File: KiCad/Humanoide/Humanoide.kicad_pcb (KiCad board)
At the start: 2 copper layers, 50 x 50 mm, 119 parts, among them CON1 SPI, IC1 CP2102, P1 CONN_01X03, P10 USB_OTG, P11 SRV9, P12 SRV10, P13 SRV11, P14 SRV12, P15 SRV13, P16 SRV14, P17 SRV15, P18 SRV16, P19 SRV17, P2 SRV1, P20 SRV18, P21 SRV19, P22 SRV20, P23 I2C, P24 UART, P25 V_BATT, P26 USB_BT, P3 SRV2, P4 SRV3, P5 SRV4, P6 SRV5, P7 SRV6, P8 SRV7, P9 SRV8, Q1 IRF7842PBF, SW1 SW_PUSH, U1 LM3940IMP, U2 ATSAM3X8EA-AU, X1 CSTCE 12MHz, Y1 32.768kHz

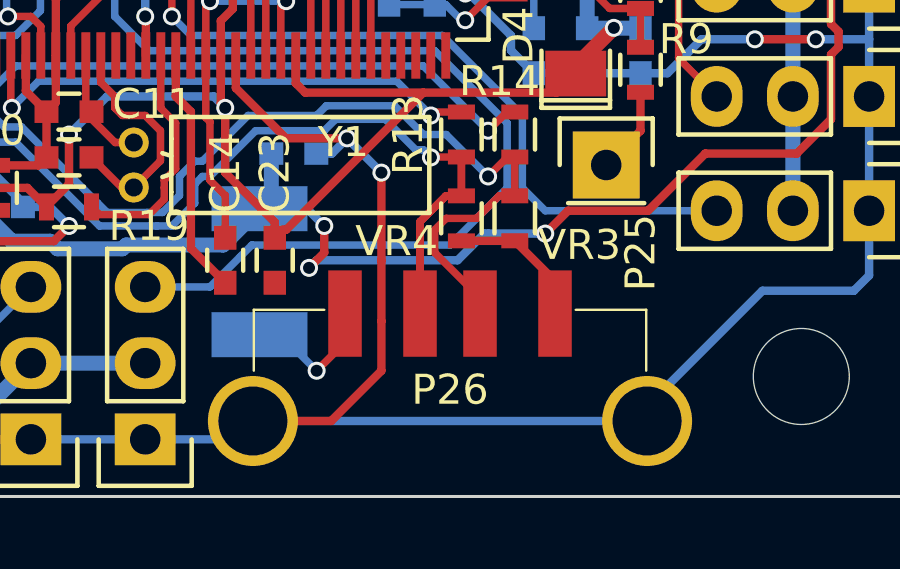
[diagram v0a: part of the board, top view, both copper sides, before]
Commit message: Kicad 3D model changed
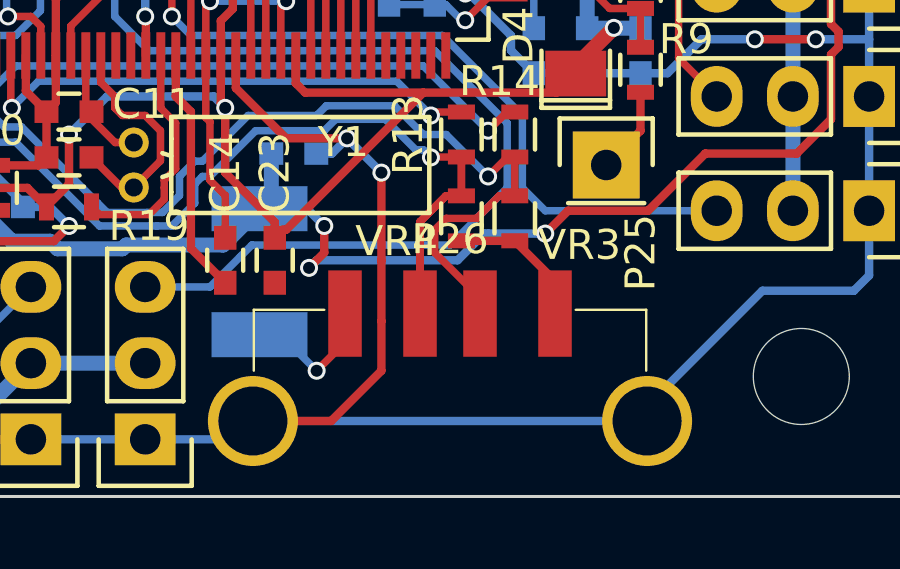
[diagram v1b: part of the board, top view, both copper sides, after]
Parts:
- P26: footprint Humanoide_lib:USB-B -> Humanoide_lib:USB-A-SMD
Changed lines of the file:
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@@
     (pad 2 smd rect (at 1.6525 0 270) (size 0.762 1.27) (layers B.Cu B.Paste B.Mask)
       (net 1 VCC))
-    (model "${KIPRJMOD}/shapes3D/diodo SS1P3L.wrl"
+    (model ${KIPRJMOD}/shapes3D/SS1P3L.wrl
       (at (xyz 0.077 0.045 0))
       (scale (xyz 0.3937 0.3937 0.3937))
@@
     (pad 2 smd rect (at 0 -2.1 270) (size 3.2 1.5) (layers B.Cu B.Paste B.Mask)
       (net 3 +5V))
-    (model "${KIPRJMOD}/shapes3D/PTC 500mA.wrl"
-      (at (xyz -0.06378 -0.08956699999999999 0))
+    (model ${KIPRJMOD}/shapes3D/mf-msmf050.wrl
+      (at (xyz 0 0 0))
       (scale (xyz 0.3937 0.3937 0.3937))
-      (rotate (xyz 270 0 270))
+      (rotate (xyz 90 0 0))
     )
   )
@@
     (pad 2 smd rect (at 0 -2.1 180) (size 3.2 1.5) (layers B.Cu B.Paste B.Mask)
       (net 29 "Net-(F2-Pad2)"))
-    (model "${KIPRJMOD}/shapes3D/PTC 500mA.wrl"
-      (at (xyz -0.06378 -0.08956699999999999 0))
+    (model ${KIPRJMOD}/shapes3D/mf-msmf050.wrl
+      (at (xyz 0 0 0))
       (scale (xyz 0.3937 0.3937 0.3937))
-      (rotate (xyz 270 0 270))
+      (rotate (xyz 90 0 0))
     )
   )
@@
     (pad 2 smd rect (at 1.35 0) (size 1.5 1.3) (layers B.Cu B.Paste B.Mask)
       (net 4 GND))
-    (model ${KIPRJMOD}/shapes3D/SMD-0805.wrl
-      (at (xyz 0 0 0))
-      (scale (xyz 0.1 0.1 0.1))
+    (model ${KIPRJMOD}/shapes3D/L_0805.wrl
+      (at (xyz 0 0 0))
+      (scale (xyz 0.3937 0.3937 0.3937))
       (rotate (xyz 0 0 0))
     )
@@
     (pad 2 smd rect (at 1.35 0 180) (size 1.5 1.3) (layers B.Cu B.Paste B.Mask)
       (net 13 "Net-(C21-Pad1)"))
-    (model ${KIPRJMOD}/shapes3D/SMD-0805.wrl
-      (at (xyz 0 0 0))
-      (scale (xyz 0.1 0.1 0.1))
+    (model ${KIPRJMOD}/shapes3D/L_0805.wrl
+      (at (xyz 0 0 0))
+      (scale (xyz 0.3937 0.3937 0.3937))
       (rotate (xyz 0 0 0))
     )
@@
     (pad 2 smd rect (at 1.35 0 180) (size 1.5 1.3) (layers B.Cu B.Paste B.Mask)
       (net 14 "Net-(C28-Pad2)"))
-    (model ${KIPRJMOD}/shapes3D/SMD-0805.wrl
-      (at (xyz 0 0 0))
-      (scale (xyz 0.1 0.1 0.1))
+    (model ${KIPRJMOD}/shapes3D/L_0805.wrl
+      (at (xyz 0 0 0))
+      (scale (xyz 0.3937 0.3937 0.3937))
       (rotate (xyz 0 0 0))
     )
@@
     (pad 2 smd rect (at 1.35 0 180) (size 1.5 1.3) (layers B.Cu B.Paste B.Mask)
       (net 15 VDDUTMI))
-    (model ${KIPRJMOD}/shapes3D/SMD-0805.wrl
-      (at (xyz 0 0 0))
-      (scale (xyz 0.1 0.1 0.1))
+    (model ${KIPRJMOD}/shapes3D/L_0805.wrl
+      (at (xyz 0 0 0))
+      (scale (xyz 0.3937 0.3937 0.3937))
       (rotate (xyz 0 0 0))
     )
@@
     (pad 2 smd rect (at 1.35 0) (size 1.5 1.3) (layers B.Cu B.Paste B.Mask)
       (net 16 VDDANA))
-    (model ${KIPRJMOD}/shapes3D/SMD-0805.wrl
-      (at (xyz 0 0 0))
-      (scale (xyz 0.1 0.1 0.1))
+    (model ${KIPRJMOD}/shapes3D/L_0805.wrl
+      (at (xyz 0 0 0))
+      (scale (xyz 0.3937 0.3937 0.3937))
       (rotate (xyz 0 0 0))
     )
@@
     (pad 6 smd rect (at 3.75 2.85) (size 2.3 1.9) (layers F.Cu F.Paste F.Mask)
       (net 43 "Net-(L1-Pad1)"))
-    (model ${KIPRJMOD}/shapes3D/micro-USB-smd.wrl
-      (at (xyz -3.857874 0.012 -0.016))
+    (model ${KIPRJMOD}/shapes3D/USB-micro-B.wrl
+      (at (xyz 0 -0.105 0))
       (scale (xyz 0.3937 0.3937 0.3937))
-      (rotate (xyz 270 0 0))
+      (rotate (xyz 0 0 270))
     )
   )
@@
     (pad 4 thru_hole oval (at 7.62 0) (size 2 2.6) (drill 1.2) (layers *.Cu *.Mask F.SilkS)
       (net 67 SCL))
-    (model ${KIPRJMOD}/shapes3D/molex-4-pines.wrl
+    (model ${KIPRJMOD}/shapes3D/22-29-2041.wrl
       (at (xyz 0.15 0 0.063))
       (scale (xyz 0.3937 0.3937 0.3937))
@@
     (pad 4 thru_hole oval (at 7.62 0) (size 2 2.6) (drill 1.2) (layers *.Cu *.Mask F.SilkS)
       (net 69 TX1))
-    (model ${KIPRJMOD}/shapes3D/molex-4-pines.wrl
+    (model ${KIPRJMOD}/shapes3D/22-29-2041.wrl
       (at (xyz 0.15 0 0.063))
       (scale (xyz 0.3937 0.3937 0.3937))
@@
       (scale (xyz 1 1 1))
       (rotate (xyz 0 0 90))
-    )
-  )
-  (module Humanoide_lib:USB-B (layer F.Cu)
-    (at 159.29 123.904)
-    (descr http://docs-europe.electrocomponents.com/webdocs/0fc0/0900766b80fc0369.pdf)
-    (tags "Connector USB SMD")
-    (fp_text reference P26 (at 0 2.54) (layer F.SilkS)
-      (effects (font (size 1 1) (thickness 0.15)))
-    )
-    (fp_text value USB_BT (at 0 2.7305) (layer F.Fab) hide
-      (effects (font (size 1 1) (thickness 0.15)))
-    )
-    (fp_line (start 6.5405 13.843) (end 6.5405 5.2705) (layer Dwgs.User) (width 0.08))
-    (fp_line (start -6.5405 13.843) (end -6.5405 5.2705) (layer Dwgs.User) (width 0.08))
-    (fp_line (start 6.5405 -0.127) (end 6.5405 1.905) (layer F.SilkS) (width 0.08))
-    (fp_line (start -4.191 -0.127) (end -6.5405 -0.127) (layer F.SilkS) (width 0.08))
-    (fp_line (start -6.5405 -0.127) (end -6.5405 1.905) (layer F.SilkS) (width 0.08))
-    (fp_line (start 6.5405 -0.127) (end 4.191 -0.127) (layer F.SilkS) (width 0.08))
-    (fp_line (start 6.5405 13.843) (end -6.5405 13.843) (layer Dwgs.User) (width 0.08))
-    (pad 1 smd rect (at -3.5 0) (size 1.12 2.88) (layers F.Cu F.Paste F.Mask)
-      (net 29 "Net-(F2-Pad2)"))
-    (pad 2 smd rect (at -1 0) (size 1.12 2.88) (layers F.Cu F.Paste F.Mask)
-      (net 71 D-))
-    (pad 3 smd rect (at 1 0) (size 1.12 2.88) (layers F.Cu F.Paste F.Mask)
-      (net 72 D+))
-    (pad 4 smd rect (at 3.5 0) (size 1.12 2.88) (layers F.Cu F.Paste F.Mask)
-      (net 4 GND))
-    (pad 5 thru_hole circle (at -6.57 3.58) (size 3 3) (drill 2.3) (layers *.Cu *.Mask F.SilkS)
-      (net 4 GND))
-    (pad 5 thru_hole circle (at 6.57 3.58) (size 3 3) (drill 2.3) (layers *.Cu *.Mask F.SilkS)
-      (net 4 GND))
-    (model ${KIPRJMOD}/shapes3D/USB_A_SMD.wrl
-      (at (xyz 0 -0.23 0.08))
-      (scale (xyz 3 3 3))
-      (rotate (xyz 270 0 0))
     )
   )
@@
     (pad 3 smd rect (at 1.2 0 270) (size 0.6 2) (layers F.Cu F.Paste F.Mask)
       (net 121 "Net-(U2-Pad36)"))
-    (model "${KIPRJMOD}/shapes3D/resonador CSTCC.wrl"
-      (at (xyz -0.06299 0.0256 0))
-      (scale (xyz 0.17 0.1778 0.170603))
-      (rotate (xyz -90 0 0))
+    (model ${KIPRJMOD}/shapes3D/CSTCE.wrl
+      (at (xyz 0 0 0))
+      (scale (xyz 400 400 400))
+      (rotate (xyz 0 0 0))
     )
   )
@@
     (pad 2 thru_hole circle (at 0.7493 0 270) (size 1.00076 1.00076) (drill 0.59944) (layers *.Cu *.Mask F.SilkS)
       (net 9 "Net-(C10-Pad1)"))
-    (model "${KIPRJMOD}/shapes3D/Crystal 32kHz.wrl"
-      (at (xyz 0.04 0.275 -0.08))
+    (model ${KIPRJMOD}/shapes3D/TC38H.wrl
+      (at (xyz 0 0.058 0.06))
       (scale (xyz 0.3937 0.3937 0.3937))
-      (rotate (xyz -90 0 90))
+      (rotate (xyz -90 180 180))
     )
   )
@@
     (pad 1 np_thru_hole circle (at 0 0) (size 3.2 3.2) (drill 3.2) (layers *.Cu *.Mask F.SilkS))
   )
+  (module Humanoide_lib:USB-A-SMD (layer F.Cu)
+    (at 159.29 123.904)
+    (descr http://docs-europe.electrocomponents.com/webdocs/0fc0/0900766b80fc0369.pdf)
+    (tags "Connector USB SMD")
+    (fp_text reference P26 (at 0 -2.4765) (layer F.SilkS)
+      (effects (font (size 1 1) (thickness 0.15)))
+    )
+    (fp_text value USB_BT (at 0 2.7305) (layer F.Fab)
+      (effects (font (size 1 1) (thickness 0.15)))
+    )
+    (fp_line (start 6.5405 13.843) (end 6.5405 5.2705) (layer Dwgs.User) (width 0.08))
+    (fp_line (start -6.5405 13.843) (end -6.5405 5.2705) (layer Dwgs.User) (width 0.08))
+    (fp_line (start 6.5405 -0.127) (end 6.5405 1.905) (layer F.SilkS) (width 0.08))
+    (fp_line (start -4.191 -0.127) (end -6.5405 -0.127) (layer F.SilkS) (width 0.08))
+    (fp_line (start -6.5405 -0.127) (end -6.5405 1.905) (layer F.SilkS) (width 0.08))
+    (fp_line (start 6.5405 -0.127) (end 4.191 -0.127) (layer F.SilkS) (width 0.08))
+    (fp_line (start 6.5405 13.843) (end -6.5405 13.843) (layer Dwgs.User) (width 0.08))
+    (pad 1 smd rect (at -3.5 0) (size 1.12 2.88) (layers F.Cu F.Paste F.Mask)
+      (net 29 "Net-(F2-Pad2)"))
+    (pad 2 smd rect (at -1 0) (size 1.12 2.88) (layers F.Cu F.Paste F.Mask)
+      (net 71 D-))
+    (pad 3 smd rect (at 1 0) (size 1.12 2.88) (layers F.Cu F.Paste F.Mask)
+      (net 72 D+))
+    (pad 4 smd rect (at 3.5 0) (size 1.12 2.88) (layers F.Cu F.Paste F.Mask)
+      (net 4 GND))
+    (pad 5 thru_hole circle (at -6.57 3.58) (size 3 3) (drill 2.3) (layers *.Cu *.Mask F.SilkS)
+      (net 4 GND))
+    (pad 5 thru_hole circle (at 6.57 3.58) (size 3 3) (drill 2.3) (layers *.Cu *.Mask F.SilkS)
+      (net 4 GND))
+    (model ${KIPRJMOD}/shapes3D/USB_A_SMD.wrl
+      (at (xyz 0 -0.23 0.055))
+      (scale (xyz 2.54 2.54 2.54))
+      (rotate (xyz 0 180 0))
+    )
+  )
   (dimension 50 (width 0.3) (layer Eco2.User)
